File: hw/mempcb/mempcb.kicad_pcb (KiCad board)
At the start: 2 copper layers, 100 x 100 mm, 32 parts, among them J1 RC6502_Bus, J2 0.1" 2x25, U1 JEDEC_DIP32_RAM, U2 74LS138, U3 74LS138

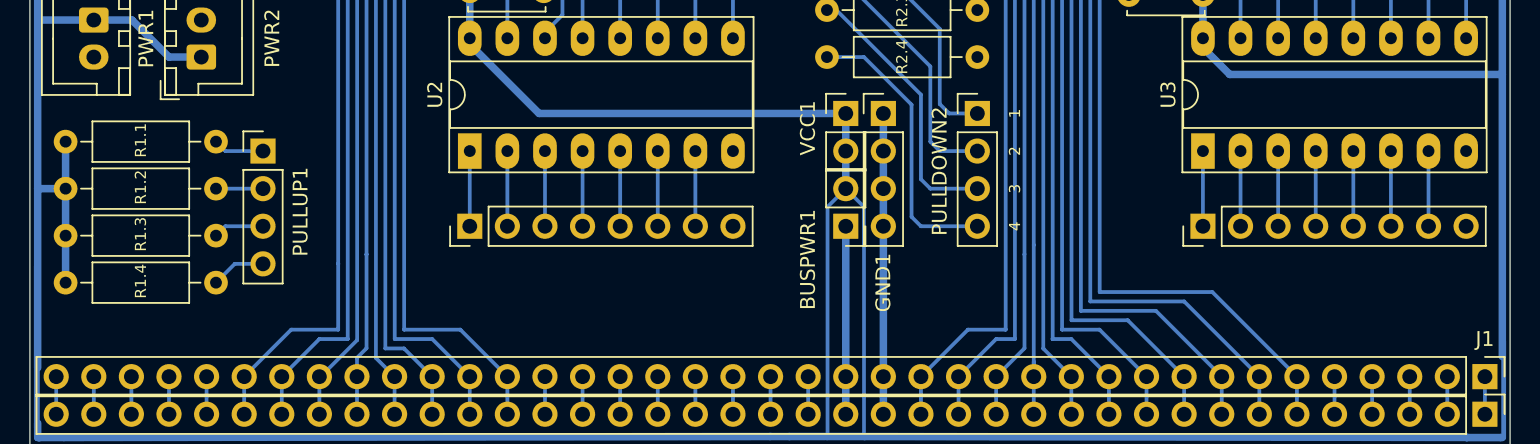
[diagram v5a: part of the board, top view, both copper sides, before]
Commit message: hw/mempcb: Update RC6502 bus connector footprint with our new one
TODO: There are still issues here with the names, such as the bus power pin
being misleading labeled VCC rather than BUS_VCC (it is not on the VCC
net).

(The new footprint in the library reduces the courtyard to the connector
edges so that bus headers can be adjacent without a warning and adds silks
for the signal names.)
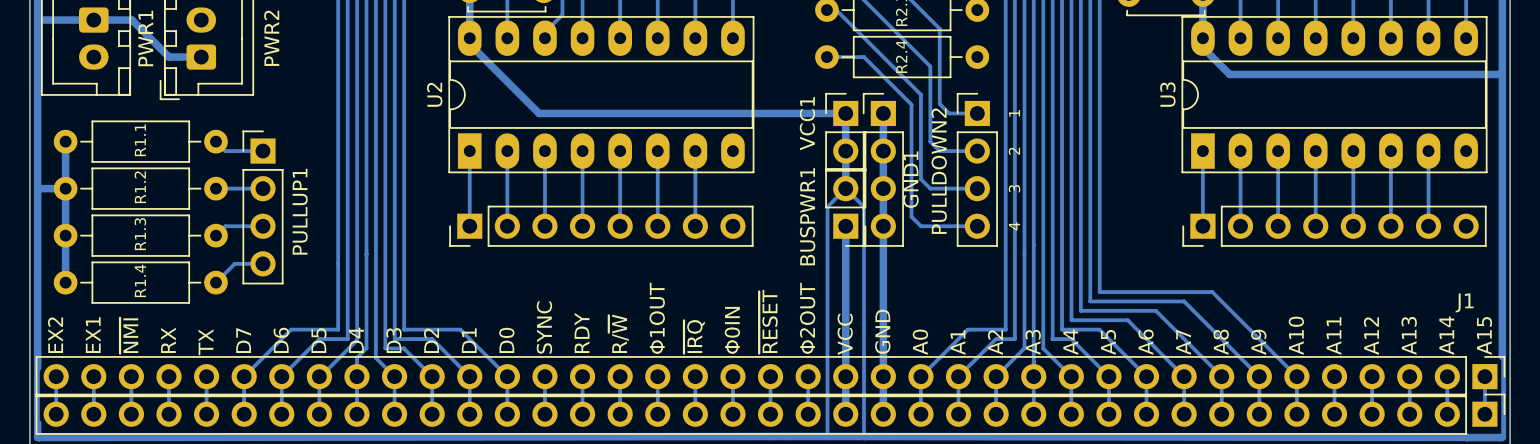
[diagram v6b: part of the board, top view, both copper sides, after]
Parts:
- J1, WW_J1: footprint Connector_PinHeader_2.54mm:PinHeader_1x39_P2.54mm_Vertical -> mempcb:RC6502_PinHeader_1x39_P2.54mm_Vertical

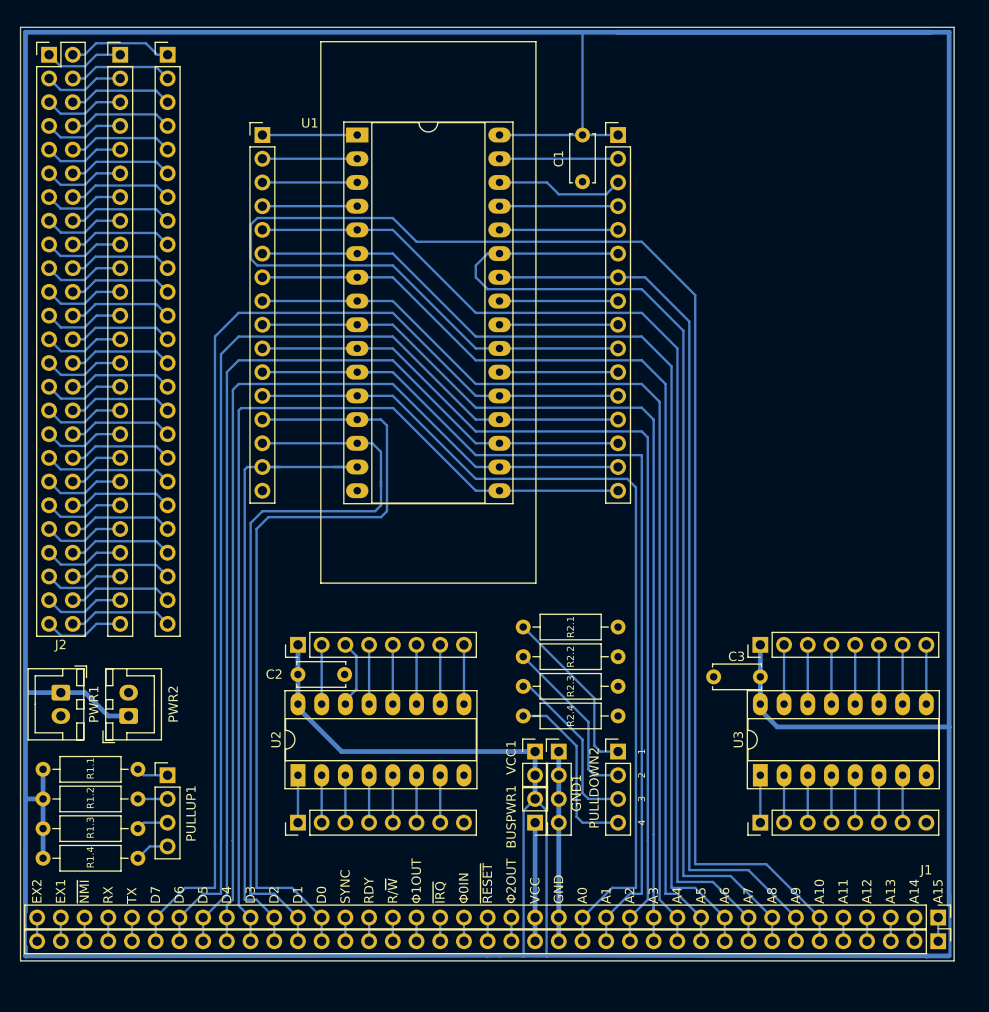
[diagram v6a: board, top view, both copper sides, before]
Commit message: ee/mempcb: Silk for memory pins
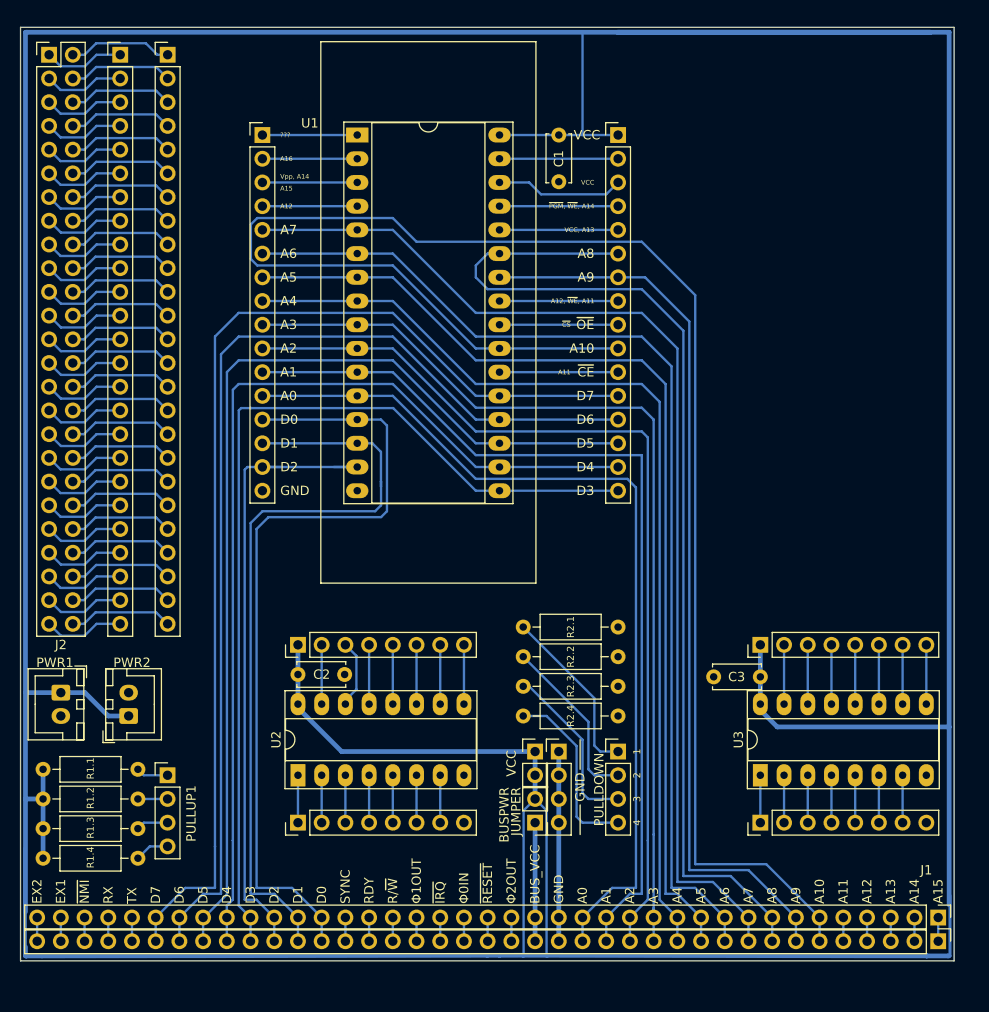
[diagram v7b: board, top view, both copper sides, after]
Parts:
- moved C1 2.54 mm to (159.4, 63.6)
